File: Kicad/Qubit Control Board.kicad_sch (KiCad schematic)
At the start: 126 parts, among them J1 USB_C_Receptacle_PowerOnly_6P, J2 CLK_Pins, J3 Idata, J4 Qdata, J5 SPIdata, J6 SMA, U2 TRF372017IRGZR, U3 LT1963AxST-3.3, U4 LT1963AxST-1.8, U5 SN65LVDS1DBV, U6 AD9743BCPZ, Y1 SiT8008xx-3x-xxN

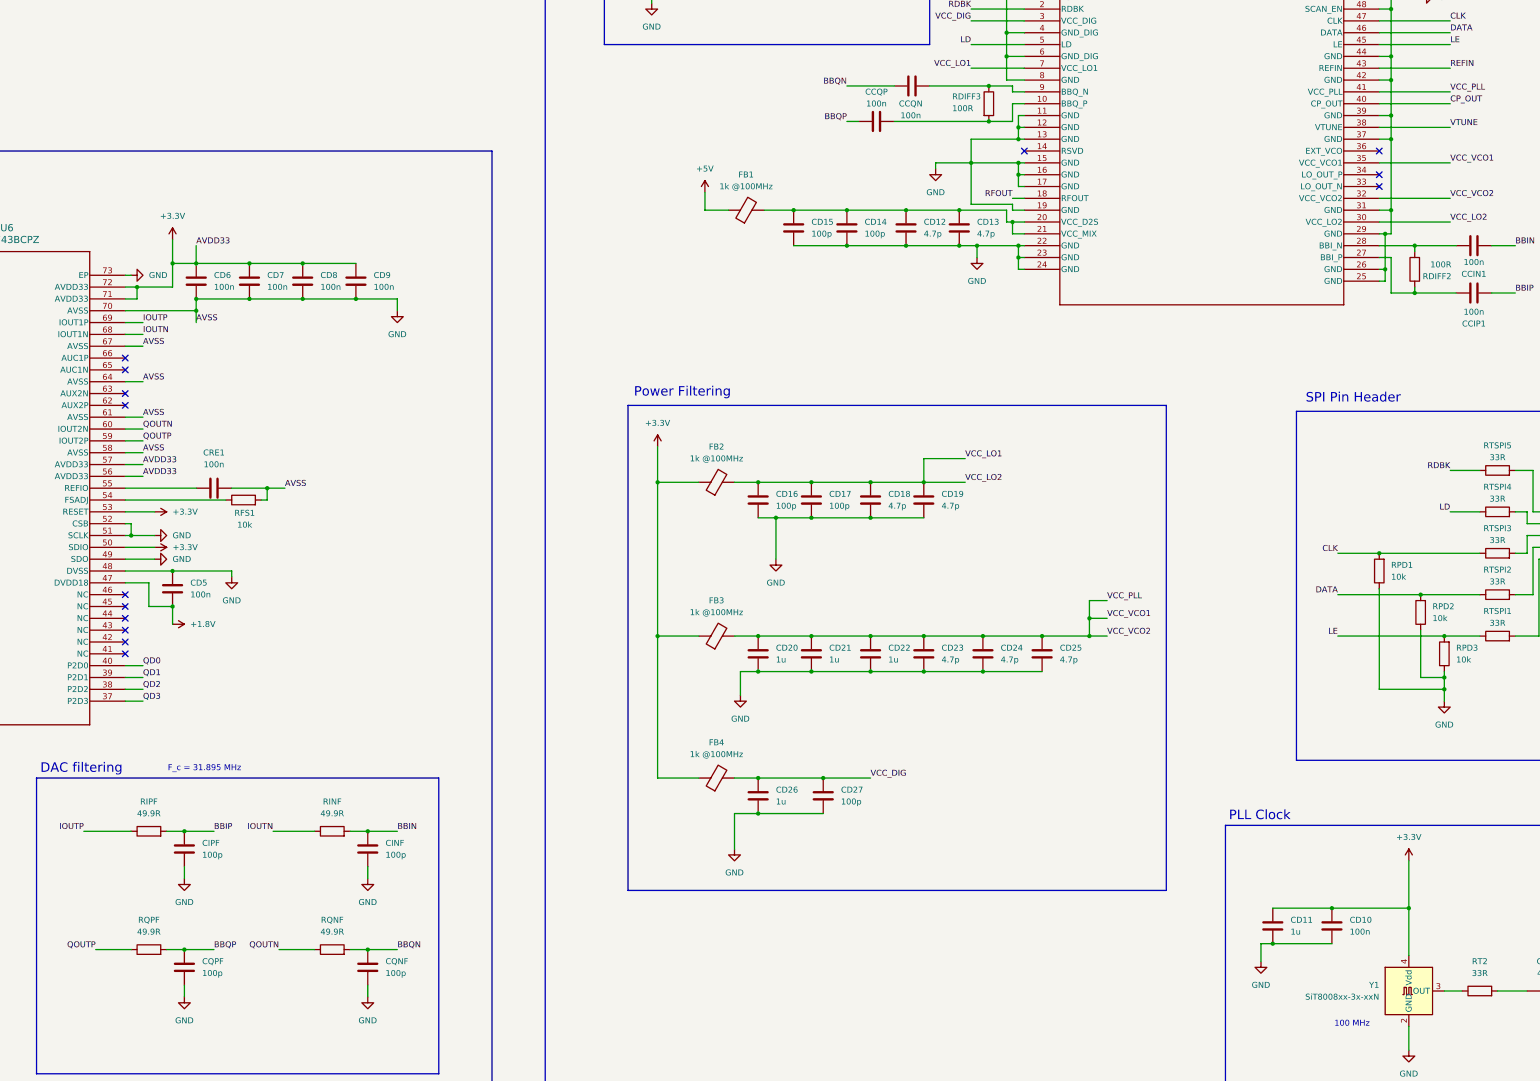
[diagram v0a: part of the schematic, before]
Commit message: added RLOAD R for the DAC post filtering
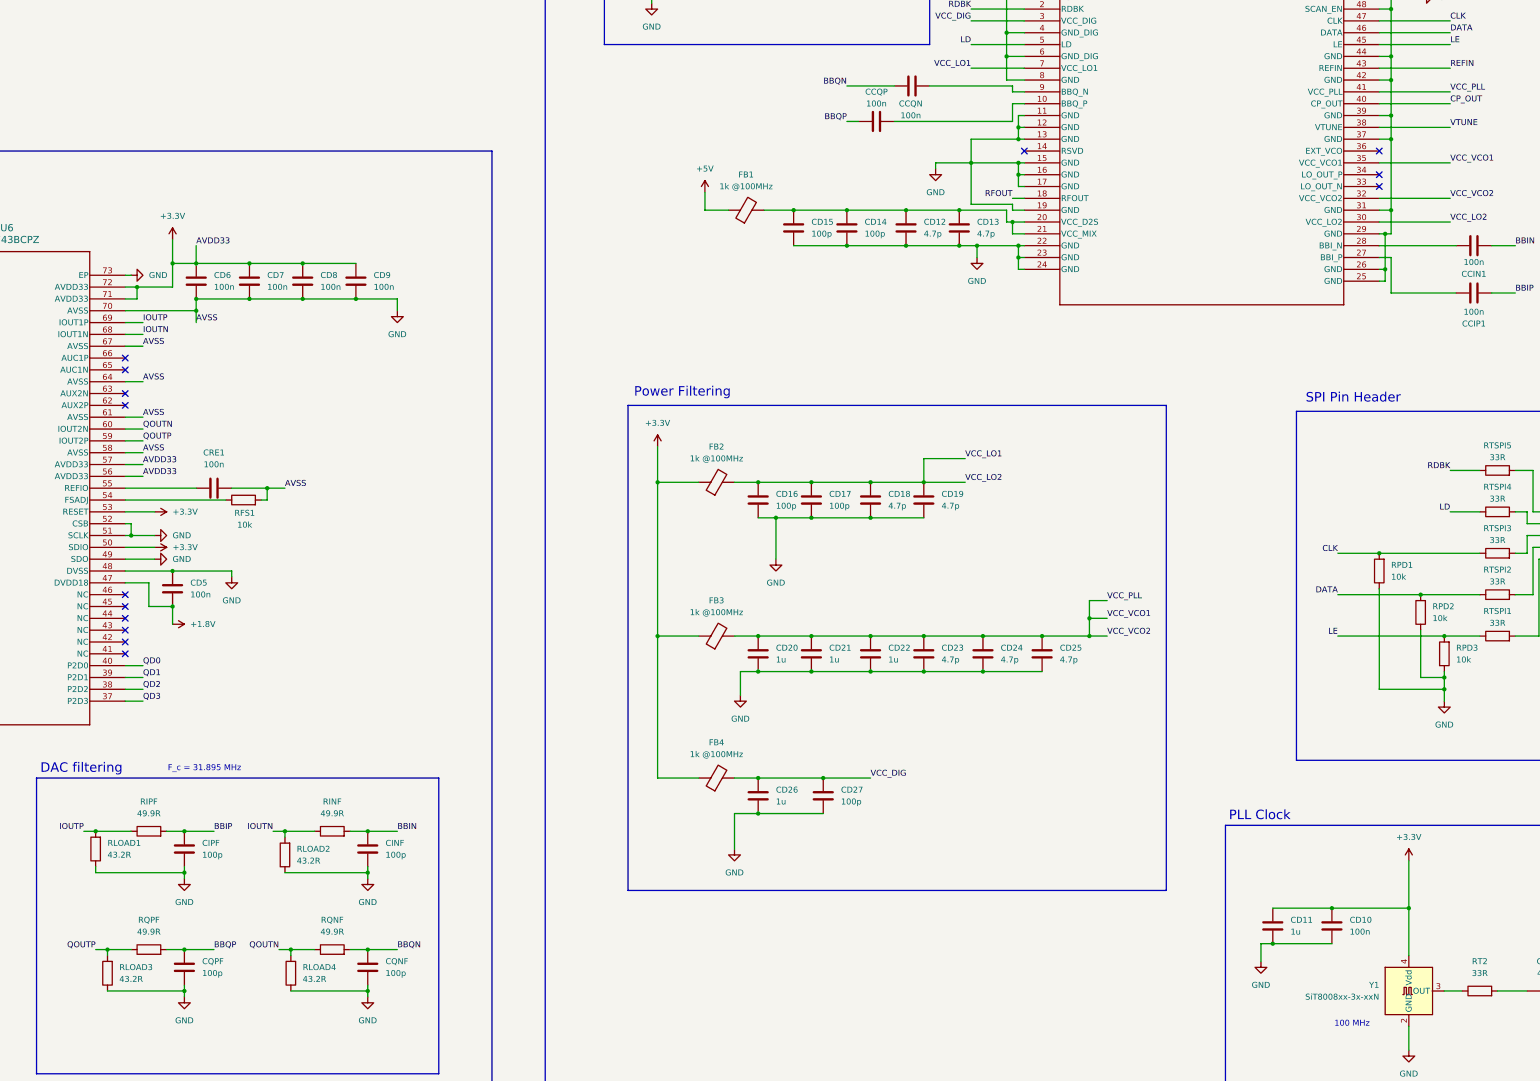
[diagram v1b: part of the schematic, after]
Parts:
- removed RDIFF2, RDIFF3: 100R, symbol Device:R
- added RLOAD1, RLOAD2, RLOAD3, RLOAD4: 43.2R, symbol Device:R
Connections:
- net GND: now also RLOAD1.1, RLOAD2.1, RLOAD3.1, RLOAD4.1
- net IOUTN: now also RLOAD2.2
- net IOUTP: now also RLOAD1.2
- net QOUTN: now also RLOAD4.2
- net QOUTP: now also RLOAD3.2
